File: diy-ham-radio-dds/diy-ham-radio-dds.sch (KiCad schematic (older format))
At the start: 52 parts, among them J1 Conn_02x03_Odd_Even, J2 Screw_Terminal_01x12, Q1 S0805, Q2 S0805, Q3 S0805, SW1 SW_Push, SW2 SW_Push, SW3 SW_Push, SW4 SW_Push, SW5 Rotary_Encoder_Switch, U1 ATmega328-AU, U2 L7805, U4 74HC595, Y1 16MHz

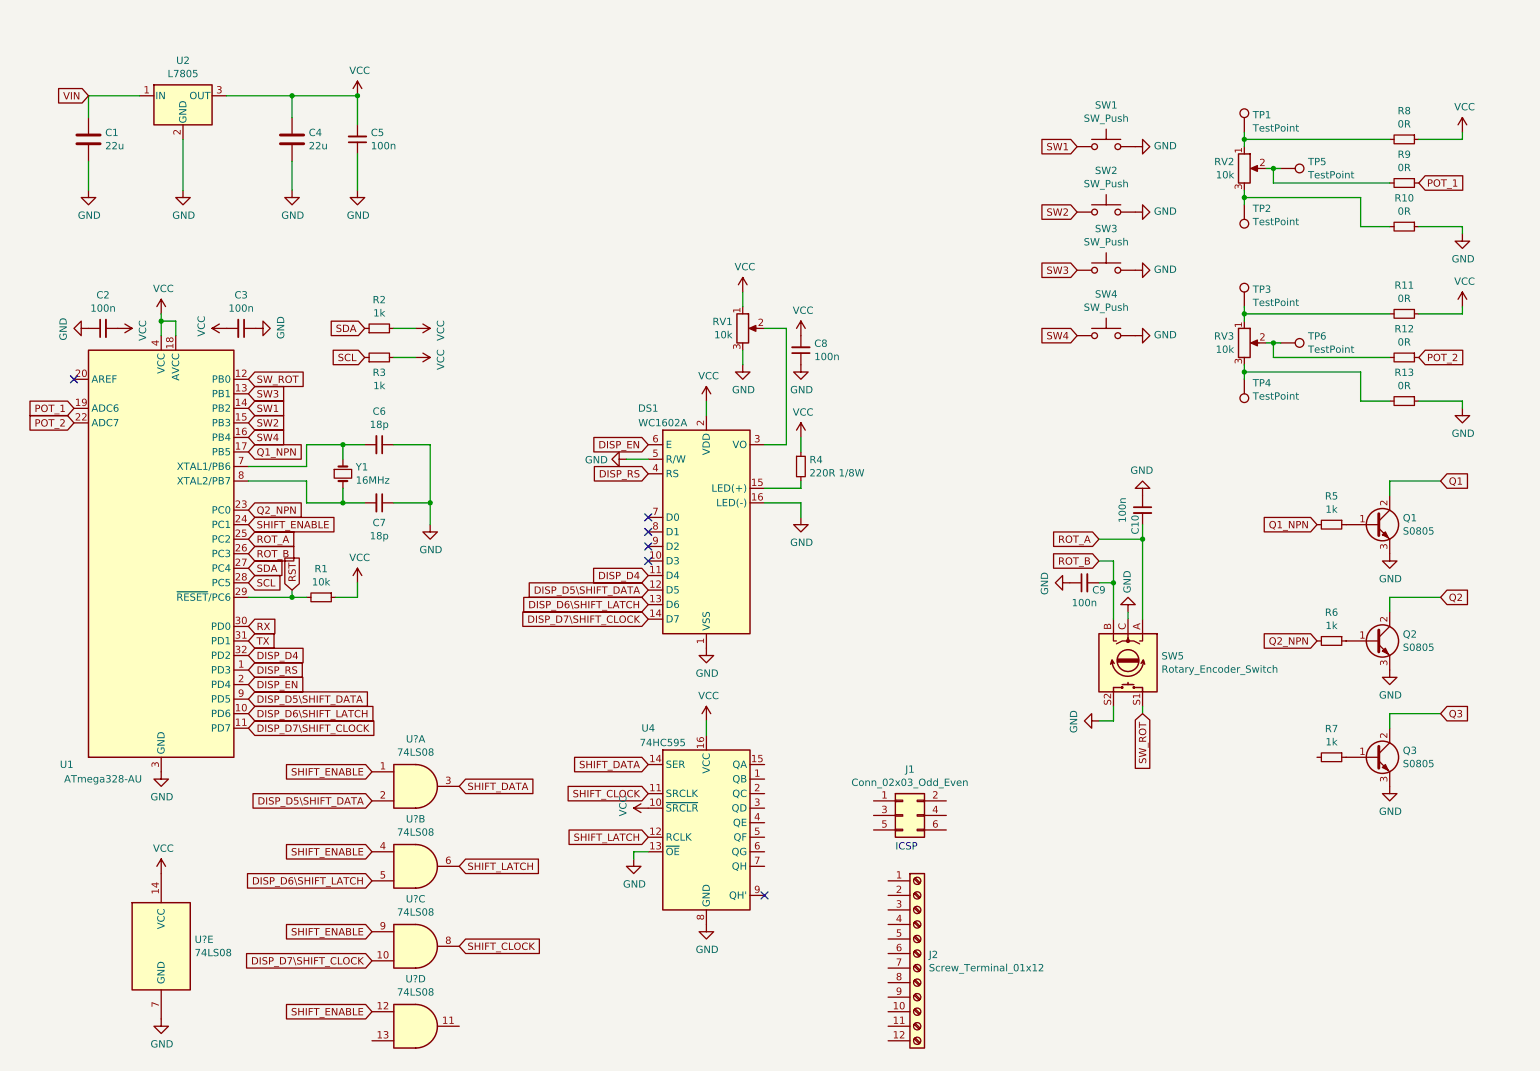
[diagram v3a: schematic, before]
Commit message: Assigned footprints to the components
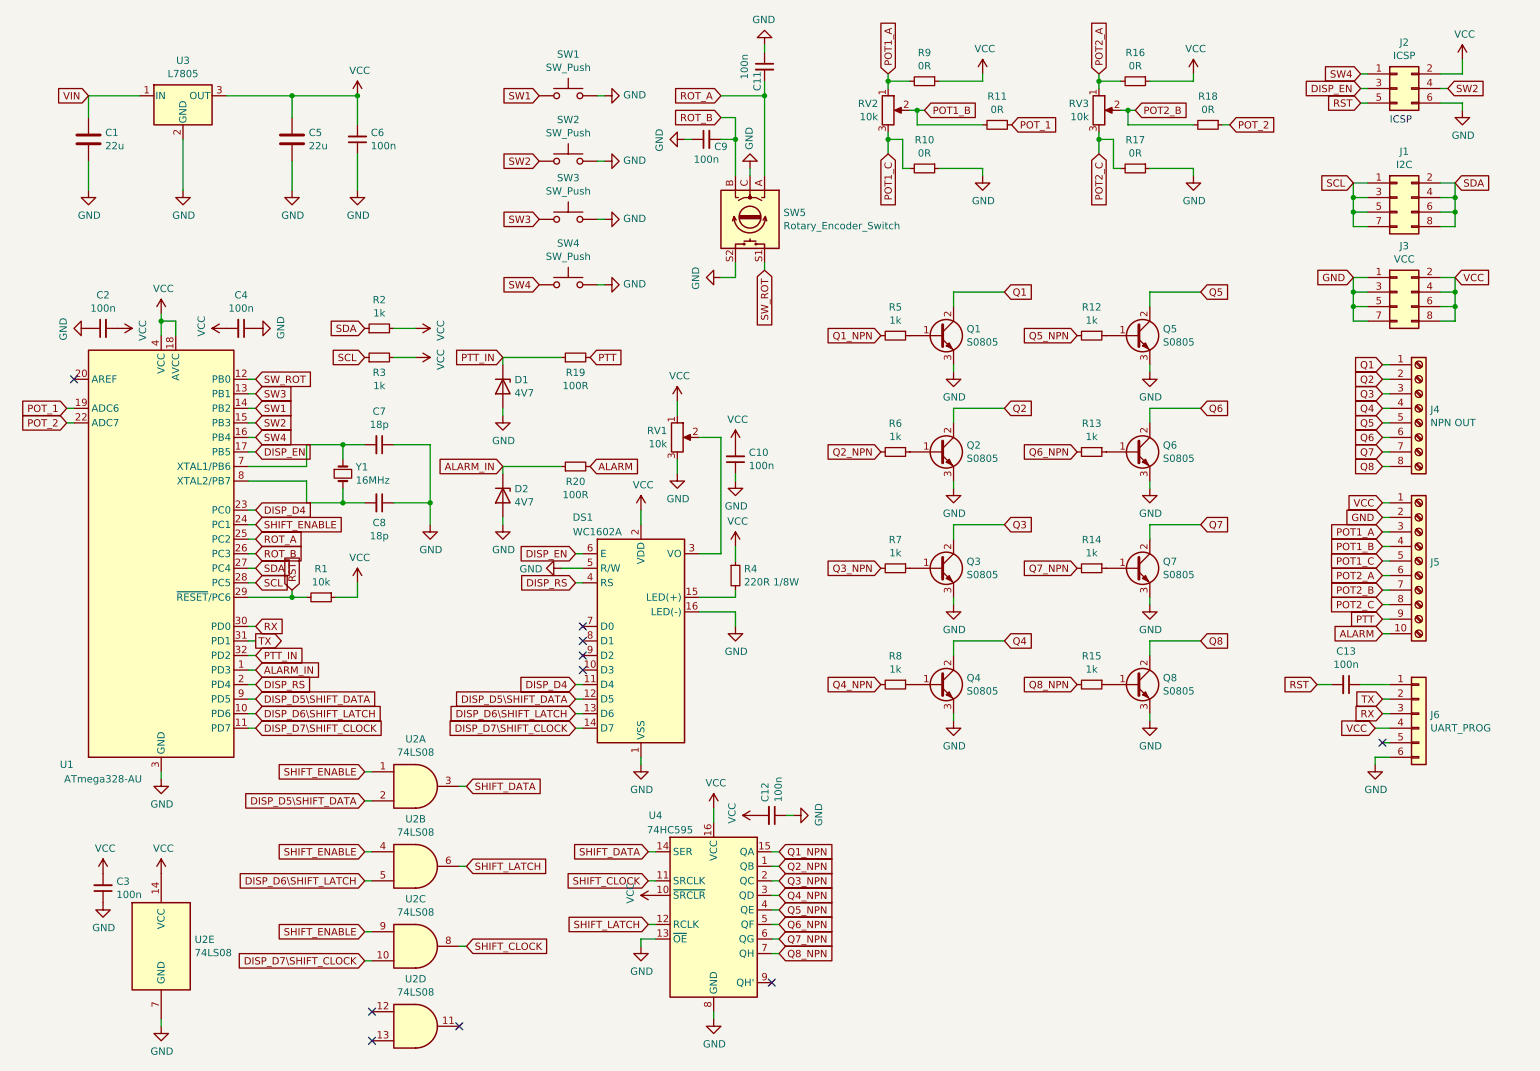
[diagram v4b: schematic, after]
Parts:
- removed J2: Screw_Terminal_01x12, symbol Connector:Screw_Terminal_01x12
- removed R11: 0R, symbol Device:R_Small
- removed TP1, TP2, TP3, TP4, TP5, TP6: TestPoint, symbol Connector:TestPoint
- added C12, C13, C3: 100n, Capacitor_SMD:C_0402_1005Metric, symbol Device:C_Small
- added D1, D2: 4V7, Diode_SMD:D_MiniMELF, symbol Device:D_Zener
- added J1: I2C, Connector_PinHeader_1.00mm:PinHeader_2x04_P1.00mm_Vertical, symbol Connector_Generic:Conn_02x04_Odd_Even
- added J3: VCC, Connector_PinHeader_1.00mm:PinHeader_2x04_P1.00mm_Vertical, symbol Connector_Generic:Conn_02x04_Odd_Even
- added J4: NPN OUT, TerminalBlock_Phoenix:TerminalBlock_Phoenix_MKDS-1,5-8-5.08_1x08_P5.08mm_Horizontal, symbol Connector:Screw_Terminal_01x08
- added J5: (no value), TerminalBlock_Phoenix:TerminalBlock_Phoenix_MKDS-3-10-5.08_1x10_P5.08mm_Horizontal, symbol Connector:Screw_Terminal_01x10
- added J6: UART_PROG, Connector_PinHeader_1.00mm:PinHeader_1x03_P1.00mm_Vertical, symbol Connector_Generic:Conn_01x06
- added Q4, Q5, Q6, Q7, Q8: S0805, Package_TO_SOT_SMD:SOT-23, symbol Device:Q_NPN_BCE
- added R14, R15: 1k, Resistor_SMD:R_0402_1005Metric, symbol Device:R_Small
- added R16, R17, R18: 0R, Resistor_SMD:R_0805_2012Metric, symbol Device:R_Small
- added R19: 100R, Resistor_SMD:R_0402_1005Metric, symbol Device:R_Small
- added R20: 100R, Resistor_SMD:R_0402_1005Metric_Pad0.72x0.64mm_HandSolder, symbol Device:R_Small
- added R8: 1k, Resistor_SMD:R_Array_Convex_4x0402, symbol Device:R_Small
- C10: renamed from C8; footprint (none) -> Capacitor_SMD:C_0402_1005Metric
- C11: renamed from C10; footprint (none) -> Capacitor_SMD:C_0402_1005Metric
- C2, C9: footprint (none) -> Capacitor_SMD:C_0402_1005Metric
- C4: renamed from C3; footprint (none) -> Capacitor_SMD:C_0402_1005Metric
- C6: renamed from C5; footprint (none) -> Capacitor_SMD:C_0402_1005Metric
- C7: renamed from C6; footprint (none) -> Capacitor_SMD:C_0402_1005Metric
- C8: renamed from C7; footprint (none) -> Capacitor_SMD:C_0402_1005Metric
- J2: renamed from J1; value Conn_02x03_Odd_Even -> ICSP; footprint (none) -> Connector_PinHeader_1.00mm:PinHeader_2x03_P1.00mm_Vertical
- Q1, Q2, Q3: footprint (none) -> Package_TO_SOT_SMD:SOT-23
- R1: footprint (none) -> Resistor_SMD:R_0402_1005Metric
- R10: footprint (none) -> Resistor_SMD:R_0805_2012Metric
- R11: renamed from R9; footprint (none) -> Resistor_SMD:R_0805_2012Metric
- R12, R13: value 0R -> 1k; footprint (none) -> Resistor_SMD:R_0402_1005Metric
- R2: footprint (none) -> Resistor_SMD:R_0402_1005Metric_Pad0.72x0.64mm_HandSolder
- R3: footprint (none) -> Resistor_SMD:R_01005_0402Metric
- R4: footprint (none) -> Resistor_SMD:R_01005_0402Metric_Pad0.57x0.30mm_HandSolder
- R5: footprint (none) -> Resistor_SMD:R_Array_Concave_4x0402
- R6: footprint (none) -> Resistor_SMD:R_Array_Convex_2x0402
- R7: footprint (none) -> Resistor_SMD:R_Array_Convex_4x0402
- R9: renamed from R8; footprint (none) -> Resistor_SMD:R_0805_2012Metric
- U2: renamed from U?; footprint (none) -> Package_SO:SOIC-14-16_3.9x9.9mm_P1.27mm
- U3: renamed from U2; footprint Package_TO_SOT_THT:TO-220-3_Horizontal_TabDown -> Package_TO_SOT_THT:TO-220-3_Vertical
- U4: footprint (none) -> Package_SO:SOIC-16_3.9x9.9mm_P1.27mm
- Y1: footprint (none) -> Crystal:Crystal_SMD_3225-4Pin_3.2x2.5mm
- renumbered C4 to C5
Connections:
- net DISP_D4: now also U1.23 (PC0); no longer U1.32 (PD2)
- net DISP_EN: now also J2.3 (Pin_3), U1.17 (PB5); no longer U1.2 (PD4)
- net DISP_RS: now also U1.2 (PD4); no longer U1.1 (PD3)
- net GND: now also J2.6 (Pin_6), C12.1, C3.1, D1.2 (A), D2.2 (A), J3.1 (Pin_1), J3.3 (Pin_3), J3.5 (Pin_5), J3.7 (Pin_7), J5.2 (Pin_2), J6.6 (Pin_6), Q4.3 (E), Q5.3 (E), Q6.3 (E), Q7.3 (E), Q8.3 (E), R17.1; no longer R13.1
- net POT_2: now also R18.1; no longer R12.1
- net Q1: now also J4.1 (Pin_1)
- net Q1_NPN: now also U4.15 (QA); no longer U1.17 (PB5)
- net Q2: now also J4.2 (Pin_2)
- net Q2_NPN: now also U4.1 (QB); no longer U1.23 (PC0)
- net Q3: now also J4.3 (Pin_3)
- net RST: now also J2.5 (Pin_5), C13.2
- net RX: now also J6.3 (Pin_3)
- net SCL: now also J1.1 (Pin_1), J1.3 (Pin_3), J1.5 (Pin_5), J1.7 (Pin_7)
- net SDA: now also J1.2 (Pin_2), J1.4 (Pin_4), J1.6 (Pin_6), J1.8 (Pin_8)
- net SHIFT_ENABLE: no longer U2.12
- net SW2: now also J2.4 (Pin_4)
- net SW4: now also J2.1 (Pin_1)
- net TX: now also J6.2 (Pin_2)
- net VCC: now also J2.2 (Pin_2), C12.2, C3.2, J3.2 (Pin_2), J3.4 (Pin_4), J3.6 (Pin_6), J3.8 (Pin_8), J5.1 (Pin_1), J6.4 (Pin_4), R16.1
- net POT1_A: now reaches R9.2, RV2.1
- net POT1_A: now also J5.3 (Pin_3)
- net POT1_B: now reaches R11.2, RV2.2
- net POT1_B: now also J5.4 (Pin_4)
- net POT1_C: now reaches R10.2, RV2.3
- net POT1_C: now also J5.5 (Pin_5)
- net Q3_NPN: now reaches U4.2 (QC)
- net Q3_NPN: now also R7.2
- net Q4_NPN: now reaches U4.3 (QD)
- net Q4_NPN: now also R8.2
- net Q5_NPN: now reaches U4.4 (QE)
- net Q5_NPN: now also R12.2
- net Q6_NPN: now reaches U4.5 (QF)
- net Q6_NPN: now also R13.2
- net Q7_NPN: now reaches U4.6 (QG)
- net Q7_NPN: now also R14.2
- net Q8_NPN: now reaches U4.7 (QH)
- net Q8_NPN: now also R15.2
- net POT2_A: now reaches RV3.1
- net POT2_A: now also J5.6 (Pin_6), R16.2
- net POT2_B: now reaches RV3.2
- net POT2_B: now also J5.7 (Pin_7), R18.2; no longer R12.2
- net POT2_C: now reaches RV3.3
- net POT2_C: now also J5.8 (Pin_8), R17.2; no longer R13.2
- new net: Q5.1 (B), R12.1
- new net: Q6.1 (B), R13.1
- new net: Q7.1 (B), R14.1
- new net: Q4.1 (B), R8.1
- new net: Q8.1 (B), R15.1
- new net: C13.1, J6.1 (Pin_1)
- new net ALARM: J5.10 (Pin_10), R20.2
- new net ALARM_IN: D2.1 (K), R20.1, U1.1 (PD3)
- new net PTT: J5.9 (Pin_9), R19.2
- new net PTT_IN: D1.1 (K), R19.1, U1.32 (PD2)
- new net Q4: J4.4 (Pin_4), Q4.2 (C)
- new net Q5: J4.5 (Pin_5), Q5.2 (C)
- new net Q6: J4.6 (Pin_6), Q6.2 (C)
- new net Q7: J4.7 (Pin_7), Q7.2 (C)
- new net Q8: J4.8 (Pin_8), Q8.2 (C)
- no-connect marks 6 -> 10
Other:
- moved on the sheet: C10, C11, C9, DS1, J2, Q1, Q2, Q3, R10, R11, R4, R5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

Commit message: Fixed wrong footprints
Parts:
- J4: footprint TerminalBlock_Phoenix:TerminalBlock_Phoenix_MKDS-1,5-8-5.08_1x08_P5.08mm_Horizontal -> TerminalBlock_Phoenix:TerminalBlock_Phoenix_MPT-0,5-8-2.54_1x08_P2.54mm_Horizontal
- J5: footprint TerminalBlock_Phoenix:TerminalBlock_Phoenix_MKDS-3-10-5.08_1x10_P5.08mm_Horizontal -> TerminalBlock_Phoenix:TerminalBlock_Phoenix_MPT-0,5-10-2.54_1x10_P2.54mm_Horizontal
- J6: footprint Connector_PinHeader_1.00mm:PinHeader_1x03_P1.00mm_Vertical -> Connector_PinHeader_1.27mm:PinHeader_1x06_P1.27mm_Vertical
- U2: footprint Package_SO:SOIC-14-16_3.9x9.9mm_P1.27mm -> Package_SO:SOIC-14_3.9x8.7mm_P1.27mm
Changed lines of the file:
@@
 F 0 "U2" H 3300 6225 50  0000 C CNN
 F 1 "74LS08" H 3300 6134 50  0000 C CNN
-F 2 "Package_SO:SOIC-14-16_3.9x9.9mm_P1.27mm" H 3300 5900 50  0001 C CNN
+F 2 "Package_SO:SOIC-14_3.9x8.7mm_P1.27mm" H 3300 5900 50  0001 C CNN
 F 3 "http://www.ti.com/lit/gpn/sn74LS08" H 3300 5900 50  0001 C CNN
 	1    3300 5900
@@
 F 0 "U2" H 3300 6775 50  0000 C CNN
 F 1 "74LS08" H 3300 6684 50  0000 C CNN
-F 2 "Package_SO:SOIC-14-16_3.9x9.9mm_P1.27mm" H 3300 6450 50  0001 C CNN
+F 2 "Package_SO:SOIC-14_3.9x8.7mm_P1.27mm" H 3300 6450 50  0001 C CNN
 F 3 "http://www.ti.com/lit/gpn/sn74LS08" H 3300 6450 50  0001 C CNN
 	2    3300 6450
@@
 F 0 "U2" H 3300 7325 50  0000 C CNN
 F 1 "74LS08" H 3300 7234 50  0000 C CNN
-F 2 "Package_SO:SOIC-14-16_3.9x9.9mm_P1.27mm" H 3300 7000 50  0001 C CNN
+F 2 "Package_SO:SOIC-14_3.9x8.7mm_P1.27mm" H 3300 7000 50  0001 C CNN
 F 3 "http://www.ti.com/lit/gpn/sn74LS08" H 3300 7000 50  0001 C CNN
 	3    3300 7000
@@
 F 0 "U2" H 3300 7875 50  0000 C CNN
 F 1 "74LS08" H 3300 7784 50  0000 C CNN
-F 2 "Package_SO:SOIC-14-16_3.9x9.9mm_P1.27mm" H 3300 7550 50  0001 C CNN
+F 2 "Package_SO:SOIC-14_3.9x8.7mm_P1.27mm" H 3300 7550 50  0001 C CNN
 F 3 "http://www.ti.com/lit/gpn/sn74LS08" H 3300 7550 50  0001 C CNN
 	4    3300 7550
@@
 F 0 "U2" H 1780 7046 50  0000 L CNN
 F 1 "74LS08" H 1780 6955 50  0000 L CNN
-F 2 "Package_SO:SOIC-14-16_3.9x9.9mm_P1.27mm" H 1550 7000 50  0001 C CNN
+F 2 "Package_SO:SOIC-14_3.9x8.7mm_P1.27mm" H 1550 7000 50  0001 C CNN
 F 3 "http://www.ti.com/lit/gpn/sn74LS08" H 1550 7000 50  0001 C CNN
 	5    1550 7000
@@
 F 0 "J4" H 10280 3292 50  0000 L CNN
 F 1 "NPN OUT" H 10280 3201 50  0000 L CNN
-F 2 "TerminalBlock_Phoenix:TerminalBlock_Phoenix_MKDS-1,5-8-5.08_1x08_P5.08mm_Horizontal" H 10200 3300 50  0001 C CNN
+F 2 "TerminalBlock_Phoenix:TerminalBlock_Phoenix_MPT-0,5-8-2.54_1x08_P2.54mm_Horizontal" H 10200 3300 50  0001 C CNN
 F 3 "~" H 10200 3300 50  0001 C CNN
 	1    10200 3300
@@
 F 0 "J5" H 10280 4342 50  0000 L CNN
 F 1 "  " H 10280 4251 50  0000 L CNN
-F 2 "TerminalBlock_Phoenix:TerminalBlock_Phoenix_MKDS-3-10-5.08_1x10_P5.08mm_Horizontal" H 10200 4350 50  0001 C CNN
+F 2 "TerminalBlock_Phoenix:TerminalBlock_Phoenix_MPT-0,5-10-2.54_1x10_P2.54mm_Horizontal" H 10200 4350 50  0001 C CNN
 F 3 "~" H 10200 4350 50  0001 C CNN
 	1    10200 4350
@@
 F 0 "J6" H 10280 5392 50  0000 L CNN
 F 1 "UART_PROG" H 10280 5301 50  0000 L CNN
-F 2 "Connector_PinHeader_1.00mm:PinHeader_1x03_P1.00mm_Vertical" H 10200 5400 50  0001 C CNN
+F 2 "Connector_PinHeader_1.27mm:PinHeader_1x06_P1.27mm_Vertical" H 10200 5400 50  0001 C CNN
 F 3 "~" H 10200 5400 50  0001 C CNN
 	1    10200 5400

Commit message: Drawing in progress
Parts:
- removed Y1: 16MHz, Crystal:Crystal_SMD_3225-4Pin_3.2x2.5mm, symbol Device:Crystal_Small
- added Y1: 16MHz, Crystal:Crystal_SMD_3225-4Pin_3.2x2.5mm, symbol Device:Crystal_GND24_Small
- R10: renamed from R8; footprint Resistor_SMD:R_Array_Convex_4x0402 -> Resistor_SMD:R_0402_1005Metric
- R7: renamed from R5; footprint Resistor_SMD:R_Array_Concave_4x0402 -> Resistor_SMD:R_0402_1005Metric
- R8: renamed from R6; footprint Resistor_SMD:R_Array_Convex_2x0402 -> Resistor_SMD:R_0402_1005Metric
- R9: renamed from R7; footprint Resistor_SMD:R_Array_Convex_4x0402 -> Resistor_SMD:R_0402_1005Metric
- renumbered J2 to J1, J1 to J2, R9 to R11, R10 to R12, R11 to R13, R12 to R14, R13 to R15, R14 to R16, R15 to R17, R16 to R18, R17 to R19, R18 to R20, R19 to R4, R20 to R5, R4 to R6
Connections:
- net DISP_D4: now also U1.24 (PC1); no longer U1.23 (PC0)
- net GND: now also Y1.2, Y1.4
- net SHIFT_ENABLE: now also U1.23 (PC0); no longer U1.24 (PC1)
- net at C7.2, U1.7 (XTAL1/PB6): now also Y1.1
- net at C8.2, U1.8 (XTAL2/PB7): now also Y1.3
- no-connect marks 10 -> 11
